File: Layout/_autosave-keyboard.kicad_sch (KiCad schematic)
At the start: 188 parts, among them J1 Conn_01x04_Socket, J2 Conn_01x04_Socket, J3 Conn_01x04_Socket, J4 Conn_01x03_Socket, J5 Conn_01x03_Socket, J6 Conn_01x03_Socket, J7 Conn_01x04_Socket, J8 Conn_01x03_Socket

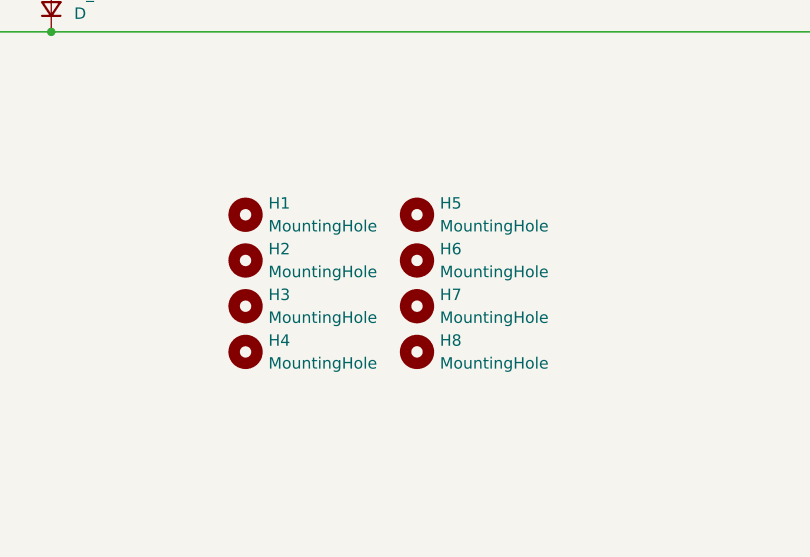
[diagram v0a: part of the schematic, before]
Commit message: PCB is done, silkscreen still needs to be done
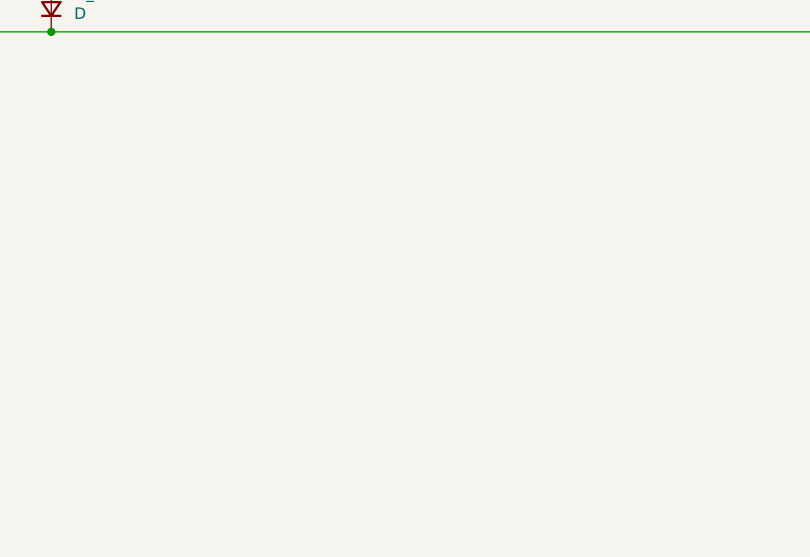
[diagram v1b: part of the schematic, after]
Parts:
- removed H1, H2, H3, H4, H5, H6, H7, H8: MountingHole, MountingHole:MountingHole_3.2mm_M3, symbol Mechanical:MountingHole
